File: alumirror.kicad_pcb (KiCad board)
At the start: 2 copper layers, 139.7 x 88.9 mm, 96 parts, among them J1 USB_C_Receptacle_USB2.0_16P_2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, J2 USB_C_Receptacle_USB2.0_16P_2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, J3 USB_C_Receptacle_USB2.0_16P_2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, J4 USB_C_Receptacle_USB2.0_16P_2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, K00 PG1350, K01 PG1350, K02 PG1350, K03 PG1350, K04 PG1350, K05 PG1350, K10 PG1350, K11 PG1350, K12 PG1350, K13 PG1350, K14 PG1350, K15 PG1350, K20 PG1350, K21 PG1350, K22 PG1350, K23 PG1350, K24 PG1350, K25 PG1350_1½U, K30 PG1350_1½U, K31 PG1350/SKQUCAA010, SW1 BOOT, U1 CH552T, U2 CH552T, U3 USBLC6-2P6, U4 USBLC6-2P6, U5 USBLC6-2P6, U6 USBLC6-2P6

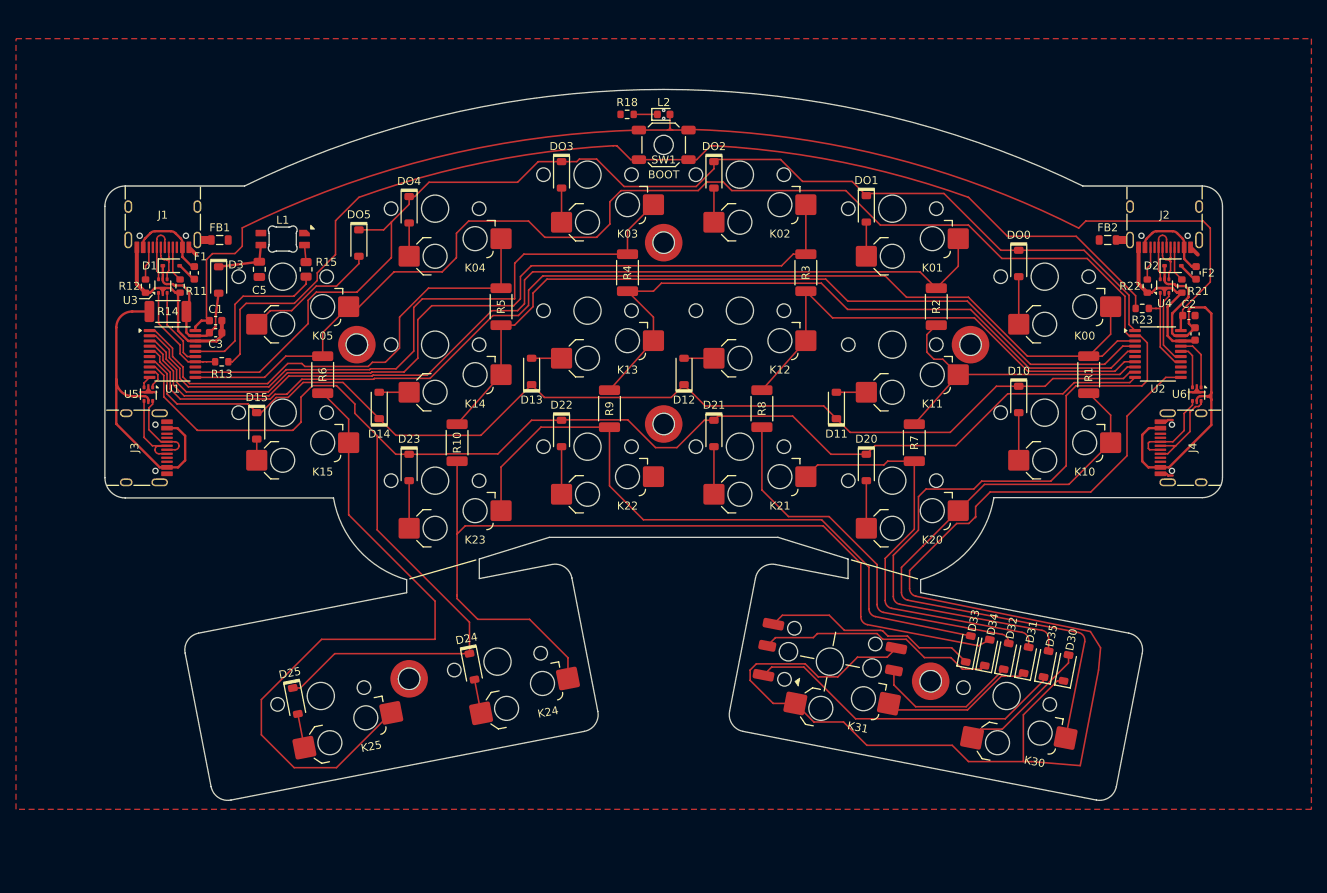
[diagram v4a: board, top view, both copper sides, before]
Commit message: Create another custom SOD-123 footprint
This one has the thicker polarity line of the existing modification, but without the 3D layer cutout.
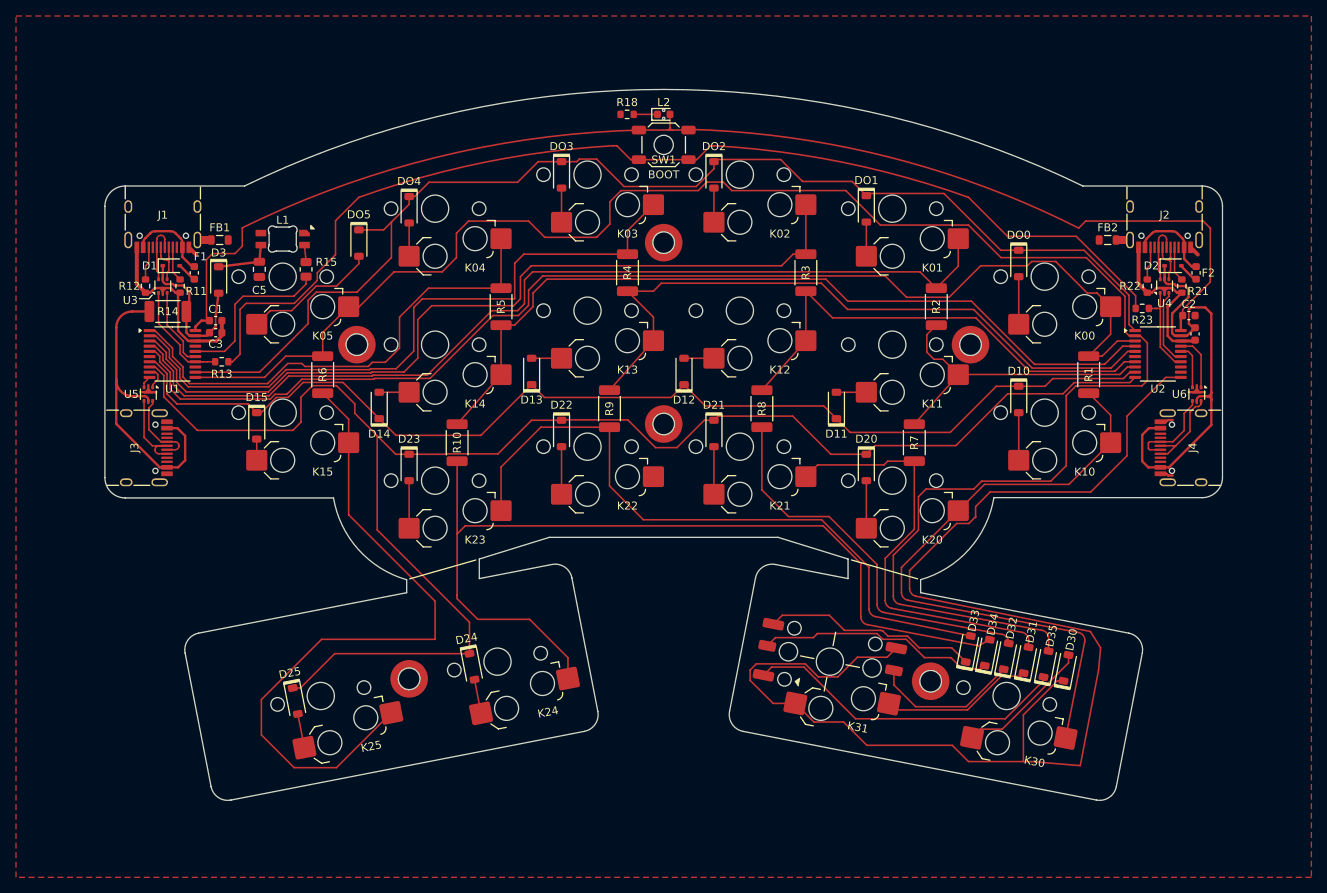
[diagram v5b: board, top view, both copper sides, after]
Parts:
- D3: footprint Project Library:D_SOD-123_Mod -> Project Library:D_SOD-123
- D30, D31, D32, D33, D34, D35: footprint Diode_SMD:D_SOD-123 -> Project Library:D_SOD-123
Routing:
- net Col0: track 147.2 -> 151.1 mm

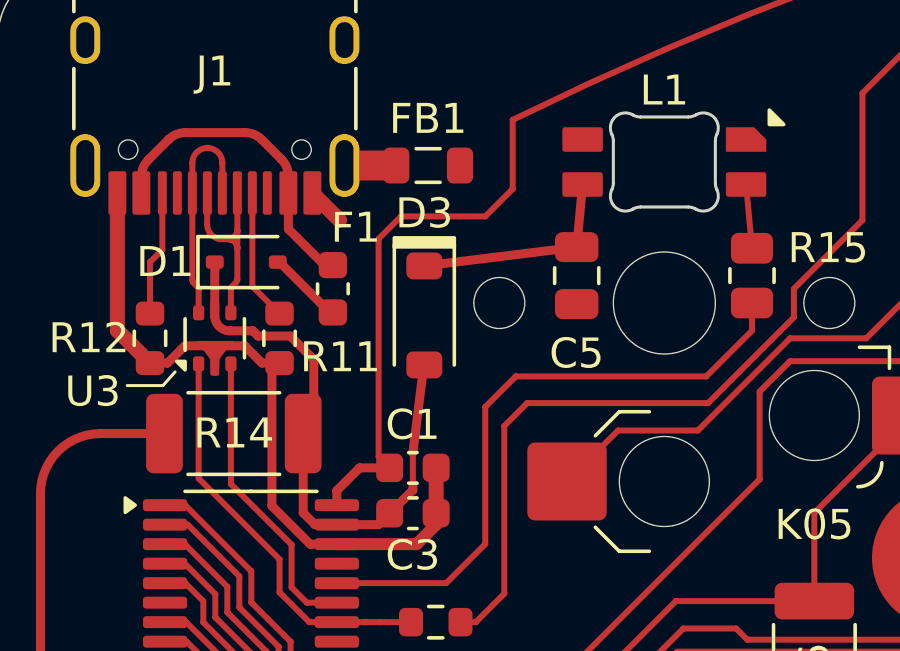
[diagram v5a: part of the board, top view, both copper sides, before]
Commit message: Change RGB LED decoupling capacitor (C5)
Use 100nF — there seems to be some contradictory information on this, but this seems to be the consensus.
Use 0603 size since the capacitance now matches C1–4, which are this size.
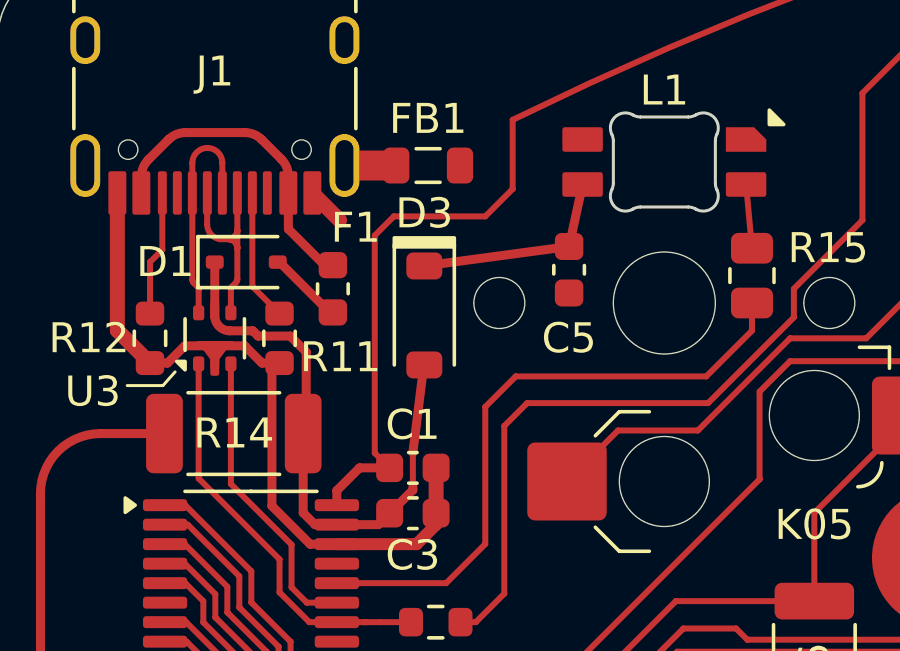
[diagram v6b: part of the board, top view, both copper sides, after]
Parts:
- C5: value 100µF -> 100nF; footprint Capacitor_SMD:C_0805_2012Metric -> Capacitor_SMD:C_0603_1608Metric
- moved C5 0.32 mm to (101.6, 51.3)

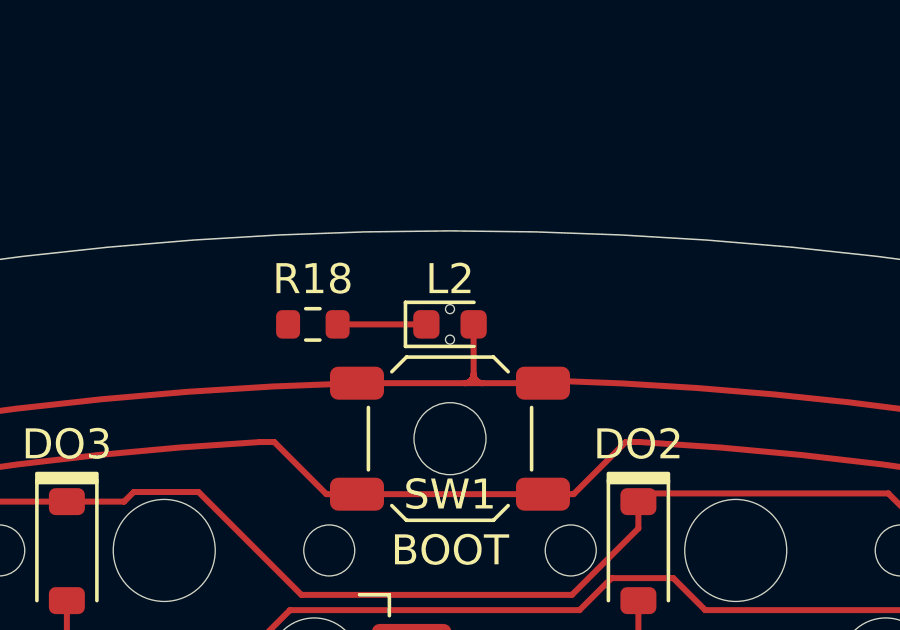
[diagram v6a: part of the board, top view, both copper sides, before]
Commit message: Change power LED to larger 0805 size
Hopefully slightly less fiddly…
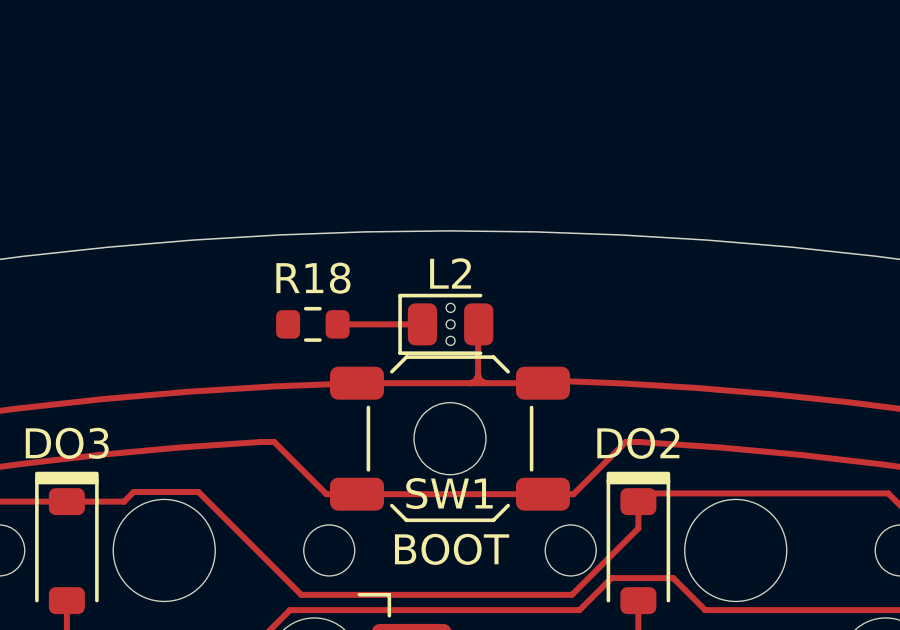
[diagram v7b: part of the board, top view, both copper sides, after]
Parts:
- L2: footprint Project Library:LED_0603_1608Metric -> Project Library:LED_0805_2012Metric_Mod
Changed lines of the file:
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@@
 		)
 	)
-	(footprint "Project Library:LED_0603_1608Metric"
+	(footprint "Project Library:LED_0805_2012Metric_Mod"
 		(layer "F.Cu")
-		(at 152.4 32.131)
-		(descr "LED SMD 0603 (1608 Metric), square (rectangular) end terminal, IPC_7351 nominal, (Body size source: http://www.tortai-tech.com/upload/download/2011102023233369053.pdf), generated with kicad-footprint-generator")
+		(at 152.42 32.131)
+		(descr "LED SMD 0805 (2012 Metric), square (rectangular) end terminal, IPC_7351 nominal, (Body size source: https://docs.google.com/spreadsheets/d/1BsfQQcO9C6DZCsRaXUlFlo91Tg2WpOkGARC1WS5S8t0/edit?usp=sharing), generated with kicad-footprint-generator")
 		(tags "LED")
 		(property "Reference" "L2"
-			(at 0 -1.504 0)
+			(at 0 -1.65 0)
 			(layer "F.SilkS")
 			(effects
@@
 		)
 		(property "Value" "LED"
-			(at 0 1.43 0)
+			(at 0 1.65 0)
 			(layer "F.Fab")
 			(effects
@@
 			)
 		)
-		(property "Footprint" "Project Library:LED_0603_1608Metric"
+		(property "Footprint" "Project Library:LED_0805_2012Metric_Mod"
 			(at 0 0 0)
 			(unlocked yes)
@@
 		(attr smd)
 		(fp_line
-			(start -1.485 -0.735)
-			(end -1.485 0.735)
+			(start -1.685 -0.96)
+			(end -1.685 0.96)
 			(stroke
 				(width 0.12)
@@
 		)
 		(fp_line
-			(start -1.485 0.735)
-			(end 0.8 0.735)
+			(start -1.685 0.96)
+			(end 1 0.96)
 			(stroke
 				(width 0.12)
@@
 		)
 		(fp_line
-			(start 0.8 -0.735)
-			(end -1.485 -0.735)
+			(start 1 -0.96)
+			(end -1.685 -0.96)
 			(stroke
 				(width 0.12)
@@
 		)
 		(fp_line
-			(start -1.48 -0.73)
-			(end 1.48 -0.73)
+			(start -1.68 -0.95)
+			(end 1.68 -0.95)
 			(stroke
 				(width 0.05)
@@
 		)
 		(fp_line
-			(start -1.48 0.73)
-			(end -1.48 -0.73)
+			(start -1.68 0.95)
+			(end -1.68 -0.95)
 			(stroke
 				(width 0.05)
@@
 		)
 		(fp_line
-			(start 1.48 -0.73)
-			(end 1.48 0.73)
+			(start 1.68 -0.95)
+			(end 1.68 0.95)
 			(stroke
 				(width 0.05)
@@
 		)
 		(fp_line
-			(start 1.48 0.73)
-			(end -1.48 0.73)
+			(start 1.68 0.95)
+			(end -1.68 0.95)
 			(stroke
 				(width 0.05)
@@
 		)
 		(fp_line
-			(start -0.8 -0.1)
-			(end -0.8 0.4)
+			(start -1 -0.3)
+			(end -1 0.6)
 			(stroke
 				(width 0.1)
@@
 		)
 		(fp_line
-			(start -0.8 0.4)
-			(end 0.8 0.4)
+			(start -1 0.6)
+			(end 1 0.6)
 			(stroke
 				(width 0.1)
@@
 		)
 		(fp_line
-			(start -0.5 -0.4)
-			(end -0.8 -0.1)
+			(start -0.7 -0.6)
+			(end -1 -0.3)
 			(stroke
 				(width 0.1)
@@
 		)
 		(fp_line
-			(start 0.8 -0.4)
-			(end -0.5 -0.4)
+			(start 1 -0.6)
+			(end -0.7 -0.6)
 			(stroke
 				(width 0.1)
@@
 		)
 		(fp_line
-			(start 0.8 0.4)
-			(end 0.8 -0.4)
+			(start 1 0.6)
+			(end 1 -0.6)
 			(stroke
 				(width 0.1)
@@
 		(fp_circle
 			(center 0 0)
-			(end 0.8 0)
+			(end 0.975 0)
 			(stroke
 				(width 0.1)
@@
 			(effects
 				(font
-					(size 0.4 0.4)
-					(thickness 0.06)
+					(size 0.5 0.5)
+					(thickness 0.08)
 				)
 			)
 		)
 		(pad "" np_thru_hole circle
-			(at 0 -0.508)
+			(at 0 -0.55)
+			(size 0.3 0.3)
+			(drill 0.3)
+			(layers "F.Mask")
+		)
+		(pad "" np_thru_hole circle
+			(at 0 0)
 			(size 0.3 0.3)
 			(drill 0.3)
@@
 		)
 		(pad "" np_thru_hole circle
-			(at 0 0.508)
+			(at 0 0.55)
 			(size 0.3 0.3)
 			(drill 0.3)
@@
 		)
 		(pad "1" smd roundrect
-			(at -0.7875 0)
-			(size 0.875 0.95)
+			(at -0.9375 0)
+			(size 0.975 1.4)
 			(layers "F.Cu" "F.Paste" "F.Mask")
 			(roundrect_rratio 0.25)
@@
 		)
 		(pad "2" smd roundrect
-			(at 0.7875 0)
-			(size 0.875 0.95)
+			(at 0.9375 0)
+			(size 0.975 1.4)
 			(layers "F.Cu" "F.Paste" "F.Mask")
 			(roundrect_rratio 0.25)
@@
 			(pintype "passive")
 		)
-		(model "${KICAD8_3DMODEL_DIR}/LED_SMD.3dshapes/LED_0603_1608Metric.wrl"
+		(model "${KICAD8_3DMODEL_DIR}/LED_SMD.3dshapes/LED_0805_2012Metric.wrl"
 			(offset
 				(xyz 0 0 0)
@@
 		(pts
 			(arc
-				(start 153.4875 34.091)
-				(mid 153.275368 34.003132)
-				(end 153.1875 33.791)
+				(start 153.6375 34.091)
+				(mid 153.425368 34.003132)
+				(end 153.3375 33.791)
 			)
 			(arc
-				(start 153.1875 33.791)
-				(mid 153.099632 34.003132)
-				(end 152.8875 34.091)
+				(start 153.3375 33.791)
+				(mid 153.249632 34.003132)
+				(end 153.0375 34.091)
 			)
 		)
@@
 	(gr_poly
 		(pts
-			(arc
-				(start 154.2 32.131)
-				(mid 153.907107 31.423893)
-				(end 153.2 31.131)
-			)
-			(arc
-				(start 151.6 31.131)
-				(mid 150.892893 31.423893)
-				(end 150.6 32.131)
-			)
-			(xy 150.6 33.131) (xy 154.2 33.12978)
+			(xy 205.74 46.430326) (xy 220.3196 46.430326) (xy 220.3196 68.58) (xy 217.932 68.58) (xy 217.932 66.548)
+			(xy 205.74 66.548)
 		)
 		(stroke
@@
 	(gr_poly
 		(pts
-			(xy 205.74 46.430326) (xy 220.3196 46.430326) (xy 220.3196 68.58) (xy 217.932 68.58) (xy 217.932 66.548)
-			(xy 205.74 66.548)
+			(arc
+				(start 154.305 31.788)
+				(mid 154.070685 31.222315)
+				(end 153.505 30.988)
+			)
+			(arc
+				(start 151.422 30.988)
+				(mid 150.856315 31.222315)
+				(end 150.622 31.788)
+			)
+			(xy 150.622 33.02) (xy 154.305 33.02)
 		)
 		(stroke
@@
 	)
 	(segment
+		(start 153.0966 34.088118)
+		(end 153.093718 34.091)
+		(width 0.2)
+		(layer "F.Cu")
+		(net 66)
+	)
+	(segment
 		(start 220.726 46.355)
 		(end 220.726 53.086)
@@
 	)
 	(segment
-		(start 153.4875 34.091)
-		(end 155.5 34.091)
+		(start 99.719001 46.312197)
+		(end 99.719001 48.616999)
 		(width 0.2)
 		(layer "F.Cu")
@@
 	)
 	(segment
-		(start 99.719001 46.312197)
-		(end 99.719001 48.616999)
+		(start 153.3375 32.131)
+		(end 153.3375 33.791)
 		(width 0.2)
 		(layer "F.Cu")
@@
 	)
 	(segment
-		(start 153.1875 32.131)
-		(end 153.1875 33.791)
+		(start 153.093718 34.091)
+		(end 149.3 34.091)
 		(width 0.2)
 		(layer "F.Cu")
@@
 	)
 	(segment
-		(start 152.8875 34.091)
-		(end 149.3 34.091)
+		(start 220.726 53.086)
+		(end 217.271 56.541)
 		(width 0.2)
 		(layer "F.Cu")
@@
 	)
 	(segment
-		(start 220.726 53.086)
-		(end 217.271 56.541)
+		(start 219.837 45.466)
+		(end 220.726 46.355)
 		(width 0.2)
 		(layer "F.Cu")
@@
 	)
 	(segment
-		(start 219.837 45.466)
-		(end 220.726 46.355)
+		(start 153.6375 34.091)
+		(end 155.5 34.091)
 		(width 0.2)
 		(layer "F.Cu")
